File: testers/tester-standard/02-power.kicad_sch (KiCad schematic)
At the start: 33 parts, among them J2 USB-C 2.0, J3 DC-005-5A-2.0, U4 CH224K, U5 USBLC6-2SC6, U6 TPS54331DR, U7 TPS54331DR

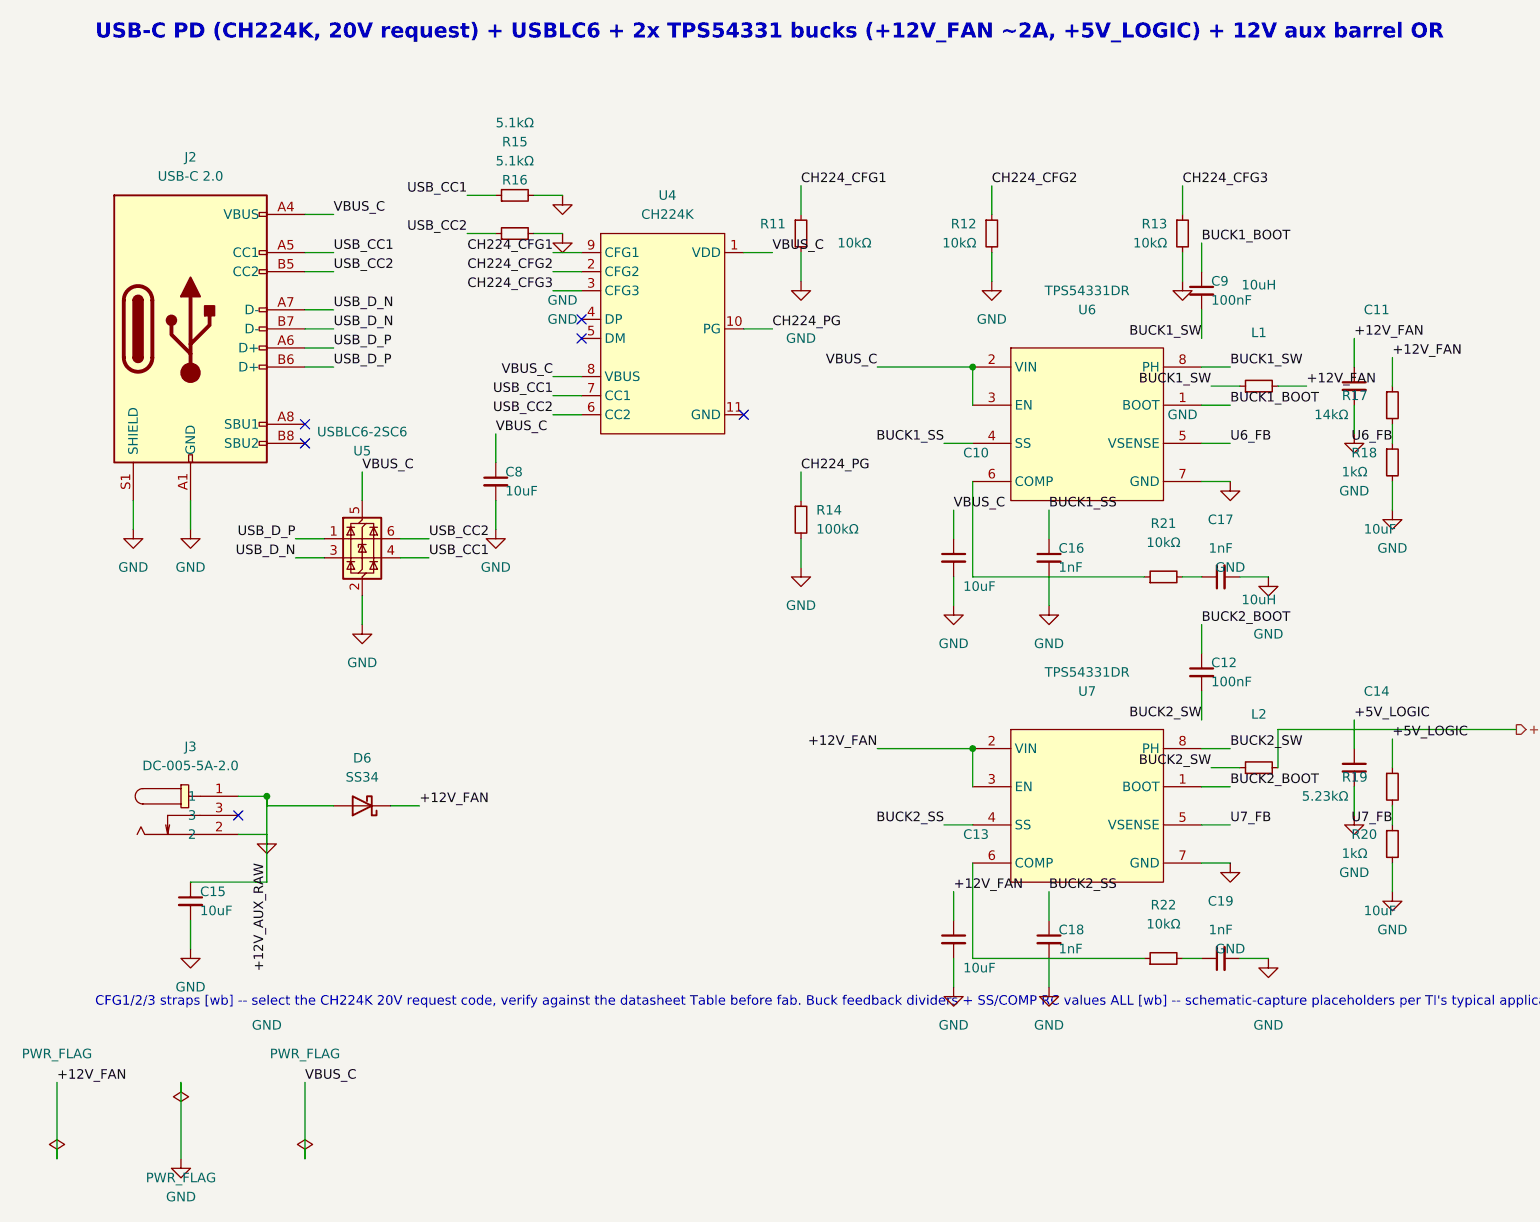
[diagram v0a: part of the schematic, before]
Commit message: tester ST Phase B: sheet 03-mcu (ESP32-C6 core + shift-register expander backbone) + a batch of real capture-time bugs found and fixed
03-mcu: ESP32-C6-MINI-1-N4 core, EN/BOOT straps, 4x PWM-setpoint RC
filters, native USB (shared with 02-power's port, global_nets) and CAN
(hier_export to 01-link), 4x 74HC595 (32 output bits: bank-group CTRL per
ladder v1.1, SCP arm x3, bay-LCD CS x6, CD4051 mux-select x3, MM74HC273
CLEAR_SHARED), 2x 74HC165 (16 input bits: 12 trip-detail + 3 fan-tach + 1
service button), 2x MM74HC273 trip-snapshot latches, CD4051 analog mux
(DETECT_SENSE relay + 6 local NTC), 3x fan headers, bimetal de-gate
backstop header. GPIO/bit budget finalized at zero spare on all three
pools (20/20 GPIO, 32/32 595 bits, 16/16 165 bits) -- flagged in
FOLLOWUPS.md.

Five real design/wiring bugs found and fixed during capture (all logged
in pin-audit-review-2026-07-16.txt addendum 5, none were in the pre-
capture design):
1. U8's GND pin-name lookup collapsed 22 physical GND pins to 1 (only
   pin 53 was ever wired) -- fixed with a proper all-pins-named lookup.
2. EN/BOOT pullup resistors wired backwards: the net table's +3V3 side
   was marked consumed with no wire, so neither pullup actually reached
   +3V3 at all.
3. `power_pin_not_driven` on +3V3/GND traced to this leaf (unlike
   01-link/02-power) having no local regulator for either rail -- both
   added to powerflag_nets.
4. MM74HC273 D-inputs were first captured tied HIGH, which would make
   every latch fire identically on any single trip -- rewired so each
   D reads its real per-source trip signal and each Q feeds the 165
   chain, restoring the intended per-leg detail capture.
5. MM74HC273 CLEAR pins were entirely unwired with no bit budgeted for
   them; freed one 595 bit by hardwiring the main LCD's CS (no bus-mate,
   needs no chip-select) instead of expanding the bit count.

Co-Authored-By: Claude Fable 5 <noreply@anthropic.com>
Claude-Session: https://claude.ai/code/session_01PhNb3Uk6THZkejvyjd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
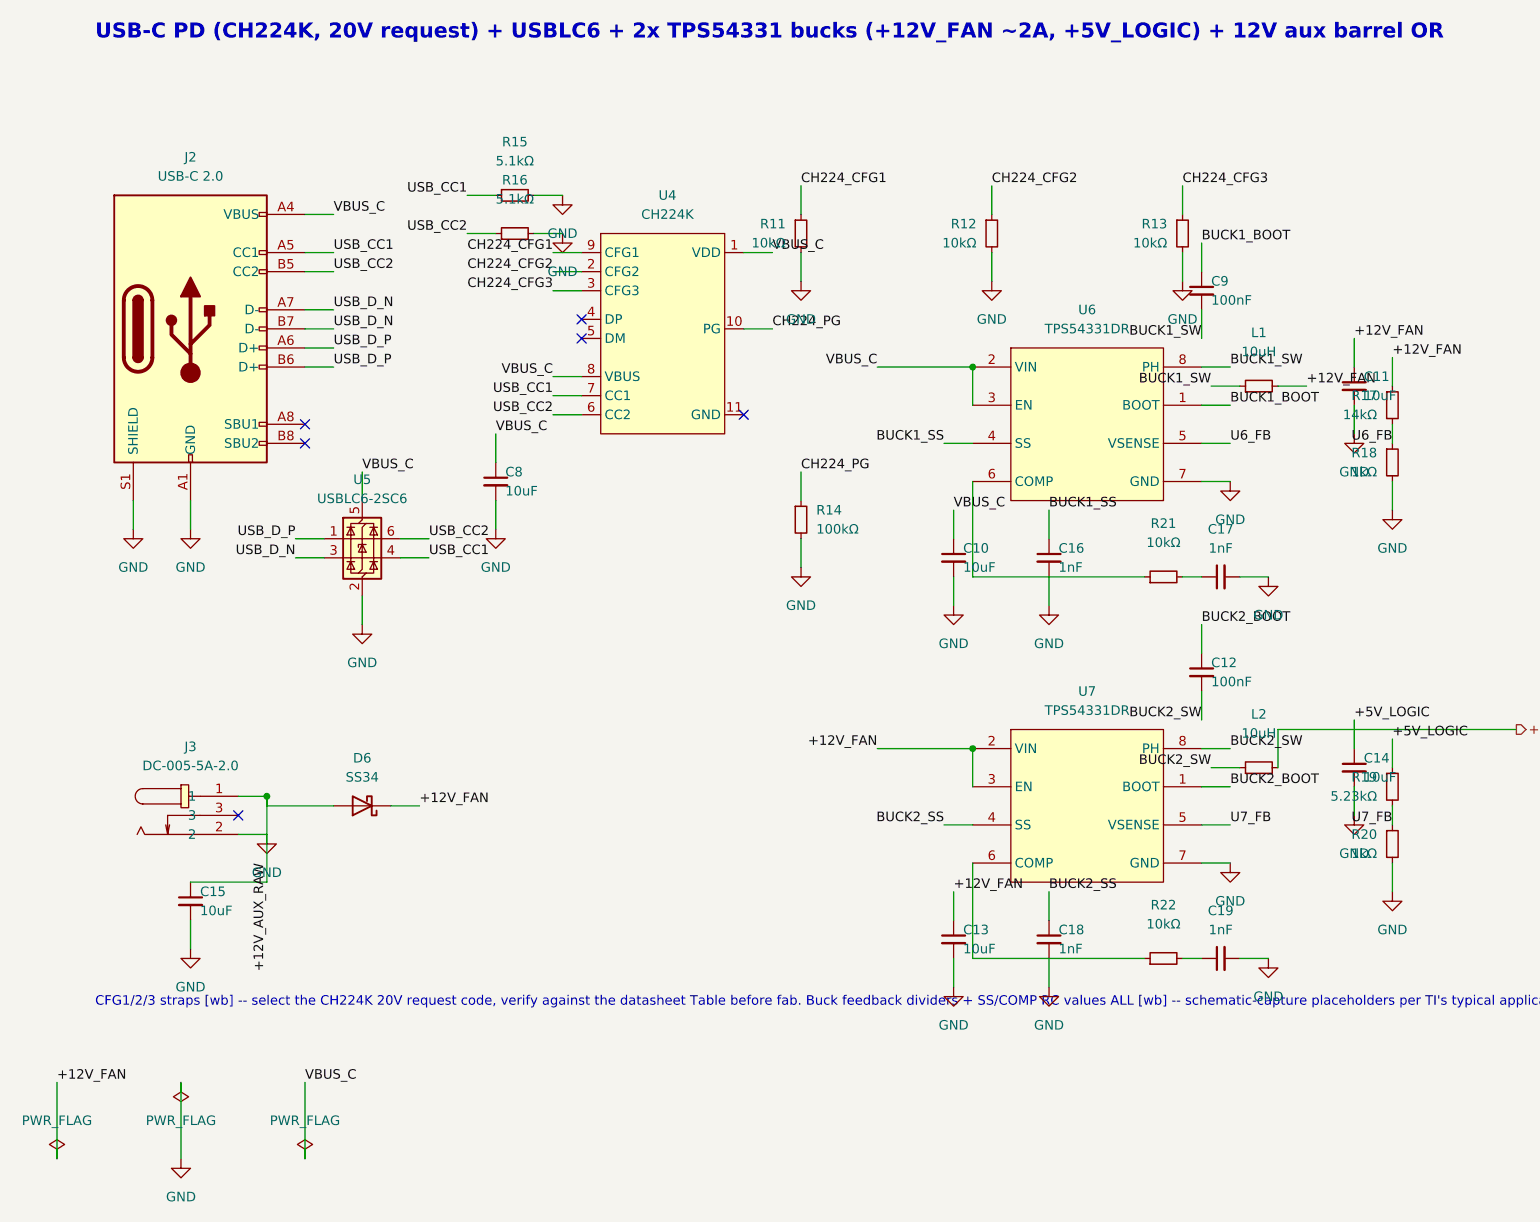
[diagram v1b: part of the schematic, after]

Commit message: tester ST: re-nudge 01-link/02-power (process gap fix, no electrical change)
The 03-mcu commit's last regeneration pass rewrote all three leaves from
source (gen_tester_st.py regenerates the whole project together) but only
re-ran cec_sch_layout.py --nudge on 03-mcu before committing, leaving
01-link/02-power's committed files in their un-nudged state (10 and 17
text overlaps respectively -- --nudge is not idempotent across a
regeneration, since regeneration rewrites from source and discards any
prior nudge, a lesson already documented in pin-audit-review-2026-07-16
.txt addendum 4 but not followed through on this specific commit). Caught
by a final verification pass across all three leaves together. Cosmetic
only: ERC and the exported netlist are unchanged (verified), only field-
text positions moved.

Co-Authored-By: Claude Fable 5 <noreply@anthropic.com>
Claude-Session: https://claude.ai/code/session_01PhNb3Uk6THZkejvyjdR4Nb
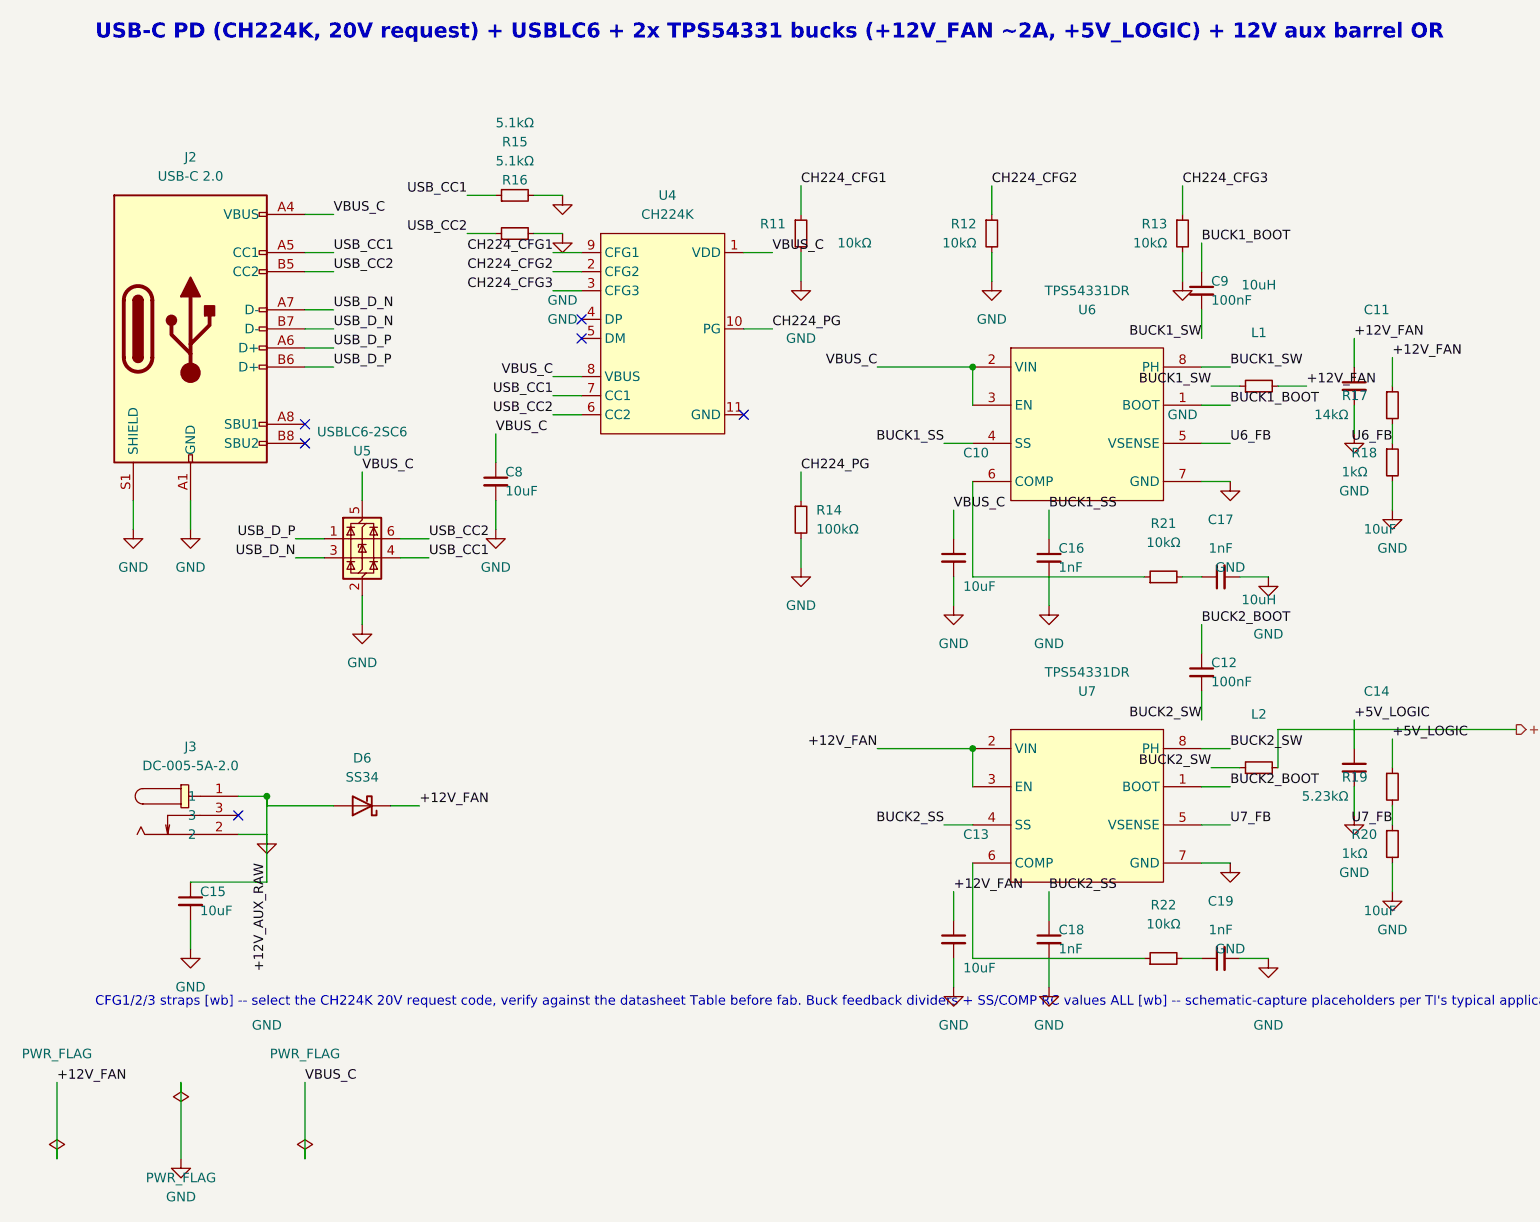
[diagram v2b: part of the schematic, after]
